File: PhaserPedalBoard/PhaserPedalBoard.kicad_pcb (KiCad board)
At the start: 4 copper layers, 114 parts, among them J1 Footswitch, J2 SWD Header, J5 In, J6 Out, J7 PowerJack, Q1 BC847, Q2 2N7002, Q4 BC847, Q5 BC857, Q6 BC857, SW1 COLOR, SW2 RST, U1 LMR62014XMF, U2 LM13700, U3 LM13700, U4 AMS1117, U5 TL074, U6 STM32L052K6T6, U7 LM2904

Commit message: routing start
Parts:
- moved R147 5.10 mm to (97.5, 84.5), turned to 0 degrees
- moved C123 3.68 mm to (118.8, 109.7)
- moved Q6 1.69 mm to (66.2, 92.3)
- moved C122 1.56 mm to (115.8, 112.1)
- moved R144 1.56 mm to (115.8, 108.8)
- moved R145 1.56 mm to (111.9, 108.8)
- moved C124 1.56 mm to (109.9, 100.9)
- moved D1 1.56 mm to (116.5, 105.3)
- moved L1 1.56 mm to (115.9, 100.6)
- moved R146 1.56 mm to (109.9, 104.8)
- moved U1 1.56 mm to (113.1, 104.8)
- moved R23 0.68 mm to (95.0, 88.0)
- moved R47 0.53 mm to (69.0, 66.0)
- moved C4 0.39 mm to (92.2, 58.5)
- moved R3 0.29 mm to (78.8, 114.0)
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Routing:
- net +3.3V: track 0.00 -> 65.8 mm
- net /Analog/VB: track 0.00 -> 59.9 mm
- net +12VA: track 0.00 -> 58.3 mm, vias 0 -> 1
- net +3.3VA: track 0.00 -> 54.9 mm
- net VCC: track 0.00 -> 36.3 mm
- net /Analog/Stg2: track 0.00 -> 28.3 mm
- net SWDIO: track 0.00 -> 27.3 mm
- net SWCLK: track 0.00 -> 24.9 mm
- net +12V: track 0.00 -> 20.3 mm
- net Net-(Q4-C): track 0.00 -> 17.2 mm
- net Net-(U3A--): track 0.00 -> 15.6 mm
- net /Digital/BypLED: track 0.00 -> 15.2 mm
- net /Analog/InGainIn: track 0.00 -> 14.8 mm
- net DAC_OUT: track 0.00 -> 14.4 mm
- net Net-(U5C-+): track 0.00 -> 13.2 mm
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- added copper zone on B.Cu, net GND
- added copper zone on F.Cu, net GND
- added copper zone on In1.Cu, net GND
- added copper zone on In2.Cu, net GND

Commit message: more routing
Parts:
- moved R26 1.97 mm to (92.8, 98.5)
- moved TP2 0.45 mm to (94.1, 112.1)
- moved R23 0.38 mm to (95.4, 87.9)
- moved R7 0.34 mm to (64.5, 111.2)
- moved R38 0.33 mm to (77.7, 109.7)
- moved R12 0.27 mm to (74.5, 95.1)
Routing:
- net /Analog/In1: track 4.08 -> 58.0 mm, vias 0 -> 3
- net /Analog/Stg4: track 0.00 -> 49.0 mm, vias 0 -> 2
- net DAC_OUT: track 14.4 -> 55.8 mm, vias 0 -> 1
- net NRST: track 3.37 -> 43.5 mm, vias 0 -> 1
- net /Analog/VB: track 59.9 -> 90.4 mm, vias 0 -> 2
- net +3.3V: track 65.8 -> 93.8 mm
- net /Analog/Stg3: track 0.00 -> 26.9 mm, vias 0 -> 2
- net /Digital/SpeedADC: track 0.00 -> 24.0 mm, vias 0 -> 2
- net Net-(U5A-+): track 0.00 -> 22.4 mm
- net Net-(SW1-C): track 0.00 -> 21.1 mm, vias 0 -> 1
- net +12VA: track 58.3 -> 77.0 mm, vias 1 -> 2
- net FX_OUT: track 0.00 -> 17.8 mm, vias 0 -> 1
- net /Analog/Stg1: track 4.63 -> 21.8 mm
- net Net-(U5D--): track 0.00 -> 8.41 mm
- net Net-(SW1-B): track 0.00 -> 7.50 mm
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
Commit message: routed, DRC passing
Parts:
- removed TP5: DAC, TestPoint:TestPoint_THTPad_D2.0mm_Drill1.0mm_VAL
- added RV3: 10kB, Potentiometer_THT:Potentiometer_Alpha_RV16AF_42_Single_Long, F.Cu at (74.1, 113.7)
- added TP3: DAC, TestPoint:TestPoint_THTPad_D2.0mm_Drill1.0mm_VAL, F.Cu at (88.0, 111.1)
- moved TP7 21.9 mm to (84.0, 76.8), turned to -90 degrees
- moved C1 11.5 mm to (104.0, 88.0), turned to -90 degrees
- moved R7 10.3 mm to (63.9, 100.8), turned to 90 degrees
- moved R30 9.97 mm to (74.3, 105.4), turned to -90 degrees
- moved R22 9.71 mm to (98.6, 78.3), turned to 90 degrees
- moved R38 8.84 mm to (72.9, 102.3), turned to 0 degrees
- moved C6 6.93 mm to (94.6, 78.2), turned to -90 degrees
- moved R20 6.88 mm to (91.0, 78.2)
- moved R21 6.88 mm to (87.7, 78.2)
- moved R23 6.88 mm to (99.0, 82.0)
- moved R24 6.88 mm to (91.1, 89.5)
- moved R25 6.88 mm to (87.7, 89.6)
- moved R27 6.88 mm to (98.6, 86.4)
- moved U3 6.88 mm to (91.5, 83.9)
- moved C14 6.88 mm to (94.6, 89.5)
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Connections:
- U5 pad 12: DAC_OUT -> Net-(U5D-+)
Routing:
- net FX_OUT: track 17.8 -> 110.3 mm, vias 1 -> 3
- net +12VA: track 77.0 -> 166.4 mm, vias 2 -> 5
- net FX_IN: track 11.5 -> 100.3 mm
- net BYP_IN: track 7.43 -> 90.9 mm, vias 0 -> 2
- net TAP_IN: track 7.75 -> 91.0 mm, vias 0 -> 2
- net /Analog/VB: track 90.4 -> 143.0 mm
- net DAC_OUT: track 55.8 -> 92.6 mm, vias 1 -> 2
- net /Analog/A: track 10.0 -> 32.9 mm, vias 0 -> 2
- net /Digital/ShapeADC: track 3.72 -> 25.1 mm, vias 0 -> 2
- net +3.3VA: track 54.9 -> 73.8 mm, vias 0 -> 1
- net Net-(U5D-+): track 0.00 -> 18.6 mm
- net /Analog/Stg4: track 49.0 -> 67.2 mm
- net NRST: track 43.5 -> 60.2 mm
- net Net-(SW1-C): track 21.1 -> 36.6 mm
- net /Analog/Stg1: track 21.8 -> 36.9 mm
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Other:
- board outline added: 61 x 80 mm

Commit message: routing tweaks
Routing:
- net /Analog/Stg4: track 67.2 -> 60.7 mm
- net /Analog/VB: track 143.0 -> 144.5 mm
- net FX_IN: track 100.3 -> 98.9 mm
- net TAP_IN: track 91.0 -> 91.6 mm
- net GND: vias 61 -> 94

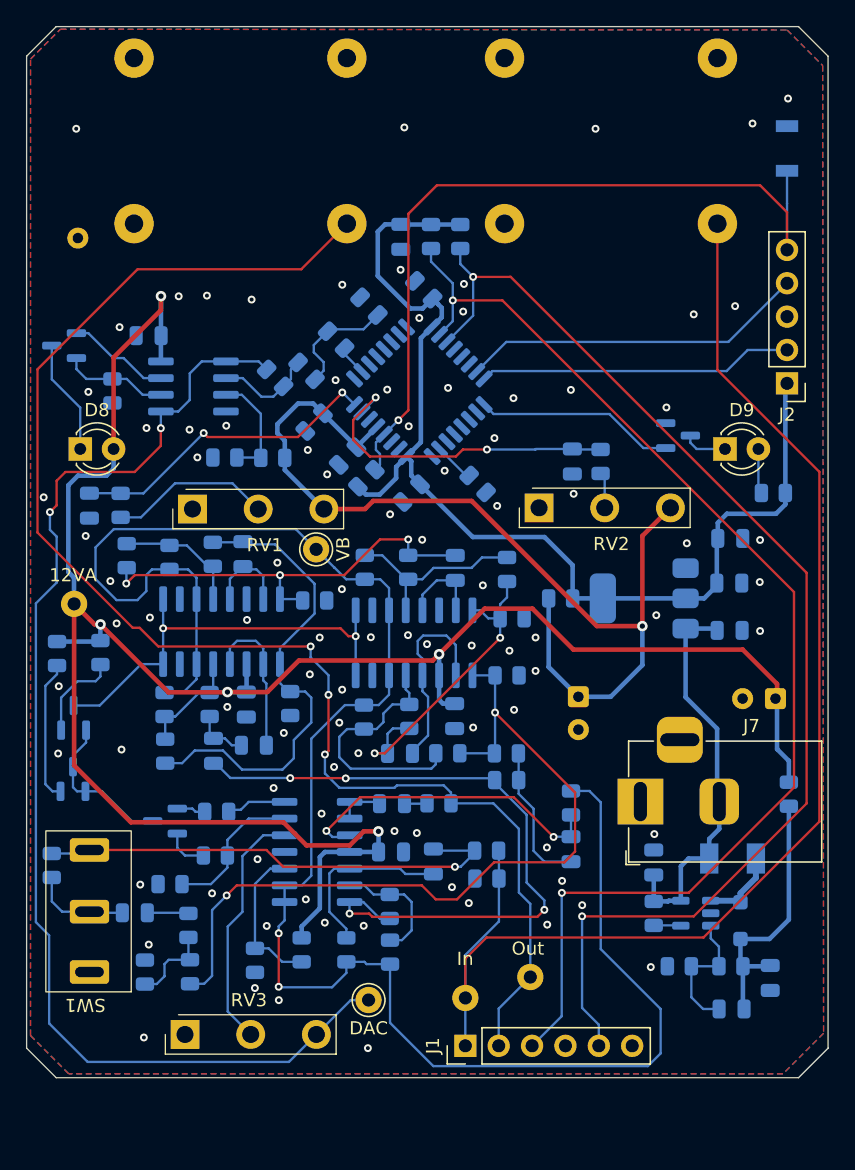
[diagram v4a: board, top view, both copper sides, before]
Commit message: tap tempo shell
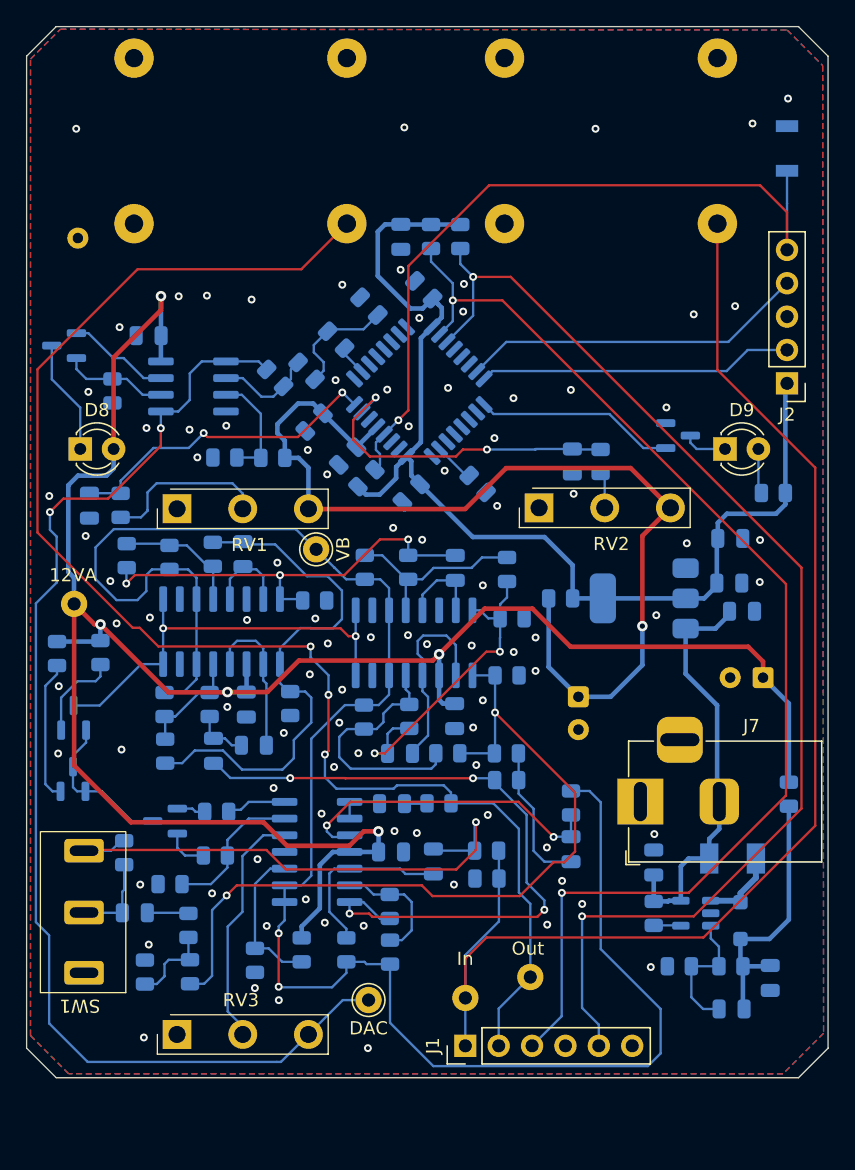
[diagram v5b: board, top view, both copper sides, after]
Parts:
- moved R7 5.59 mm to (69.4, 99.9)
- moved C12 1.86 mm to (118.0, 86.5)
- moved C18 1.73 mm to (116.5, 81.5)
- moved RV1 1.18 mm to (73.5, 73.7)
- moved RV3 0.61 mm to (73.5, 113.7)
- moved SW1 0.42 mm to (69.8, 110.8)
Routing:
- net Net-(SW1-C): track 36.6 -> 42.3 mm
- net /Analog/Stg1: track 36.9 -> 41.0 mm
- net NRST: track 60.2 -> 57.9 mm
- net +3.3VA: track 73.8 -> 75.5 mm
- net VCC: track 30.5 -> 32.0 mm
- net DAC_OUT: track 93.0 -> 91.9 mm
- net Net-(SW1-B): track 7.55 -> 6.73 mm
- net /Analog/Stg3: track 24.4 -> 25.0 mm
- net /Digital/SpeedADC: track 24.0 -> 24.6 mm
- net BYP_IN: track 91.3 -> 90.8 mm

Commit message: routing w DRC passing
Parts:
- removed C21: 10u, Capacitor_SMD:C_0805_2012Metric
- removed R42: 2k2, Resistor_SMD:R_0805_2012Metric
- removed R7: 270k, Resistor_SMD:R_0805_2012Metric
- removed SW1: COLOR, Button_Switch_THT:SW_SPDT_Dailywell_Mini_1M
- added RV4: 10kB, Potentiometer_THT:Potentiometer_Alpha_RV16AF_42_Single_Long, F.Cu at (72.3, 105.8)
- C1: value 220u -> 100u; footprint Capacitor_THT:CP_Radial_D7.5mm_P2.50mm -> Capacitor_THT:CP_Radial_D6.3mm_P2.50mm
- J7, TP3, TP7: moved to B.Cu
- R28: value 4k7 -> 3k3
- R29, R38: value 3k3 -> 4k7
- moved J8 54.2 mm to (119.1, 42.7), turned to -90 degrees
- moved Q5 53.5 mm to (118.9, 97.6)
- moved Q6 53.4 mm to (118.9, 92.8)
- moved R40 52.2 mm to (114.7, 98.3), turned to 180 degrees
- moved R41 47.9 mm to (114.6, 93.8), turned to 180 degrees
- moved Q4 47.1 mm to (119.3, 103.2), turned to 0 degrees
- moved R38 43.1 mm to (116.0, 101.3), turned to -90 degrees
- moved C12 40.1 mm to (89.3, 114.5), turned to -90 degrees
- moved R48 36.3 mm to (95.6, 44.6), turned to 90 degrees
- moved TP6 36.2 mm to (85.3, 111.3)
- moved R5 32.8 mm to (65.3, 110.3), turned to -90 degrees
- moved D9 31.8 mm to (93.0, 46.4), turned to 90 degrees
- moved R1 31.5 mm to (92.6, 110.9), turned to 180 degrees
- moved R6 30.5 mm to (68.4, 110.3), turned to 90 degrees
- moved RV3 30.2 mm to (102.5, 105.8)
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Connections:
- C3 pad 1: Net-(SW1-C) -> Net-(C3-Pad1)
- C9 pad 1: Net-(SW1-B) -> Net-(C3-Pad1)
- R10 pad 1: Net-(U5B--) -> Net-(U5D--)
- R29 pad 1: Net-(R28-Pad2) -> Net-(R29-Pad1)
- R30 pad 2: Net-(R28-Pad2) -> Net-(R30-Pad2)
- R38 pad 2: Net-(U5D--) -> Net-(Q4-E)
- R6 pad 2: Net-(SW1-C) -> Net-(C3-Pad1)
- R9 pad 2: Net-(U5B--) -> Net-(U5D--)
- RV3 pad 2: Net-(U5D-+) -> Net-(U5B-+)
- U5 pad 12: Net-(U5D-+) -> /Analog/InGainIn
- U5 pad 14: Net-(R39-Pad1) -> /Analog/In1
- U5 pad 5: /Analog/InGainIn -> Net-(U5B-+)
- U5 pad 6: Net-(U5B--) -> Net-(Q4-E)
- U5 pad 7: /Analog/In1 -> Net-(R39-Pad1)
- U6 pad 14: unconnected-(U6-PB0-Pad14) -> /Digital/BypLED
- U6 pad 25: /Digital/BypLED -> unconnected-(U6-PA15-Pad25)
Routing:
- net /Analog/A: track 32.9 -> 81.1 mm, vias 2 -> 3
- net Net-(SW1-C): track 42.3 -> 0.00 mm, vias 1 -> 0
- net FX_IN: track 98.6 -> 137.2 mm
- net DAC_OUT: track 91.9 -> 128.9 mm, vias 2 -> 1
- net /Analog/VB: track 144.5 -> 110.7 mm, vias 2 -> 4
- net VCC: track 32.0 -> 64.7 mm, vias 0 -> 1
- net NRST: track 57.9 -> 88.3 mm
- net TAP_IN: track 91.3 -> 120.4 mm, vias 2 -> 3
- net /Analog/In1: track 53.0 -> 26.4 mm, vias 4 -> 0
- net Net-(C3-Pad1): track 0.00 -> 26.3 mm
- net Net-(Q4-B): track 2.19 -> 25.8 mm
- net BYP_IN: track 90.8 -> 114.1 mm, vias 2 -> 3
- net Net-(Q4-E): track 3.31 -> 25.6 mm
- net Net-(U5D-+): track 18.6 -> 0.00 mm
- net Net-(U5B-+): track 0.00 -> 15.4 mm, vias 0 -> 1
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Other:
- board size 61 x 80 mm -> 61 x 85 mm

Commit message: minor niceties
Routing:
- net FX_IN: track 137.2 -> 140.2 mm
- net +3.3VA: track 79.1 -> 77.7 mm
- net Net-(C8-Pad2): track 11.9 -> 11.3 mm
- net GND: vias 33 -> 81

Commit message: routing improvements
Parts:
- moved Q2 0.86 mm to (92.9, 50.6)
- moved R48 0.86 mm to (95.5, 45.4)
- moved D9 0.86 mm to (92.9, 47.2)
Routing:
- net /Analog/Stg4: track 63.5 -> 59.5 mm
- net NRST: track 87.9 -> 84.5 mm, vias 1 -> 2
- net TAP_IN: track 120.4 -> 117.5 mm, vias 3 -> 1
- net FX_IN: track 140.2 -> 137.4 mm
- net /Analog/Stg1: track 30.9 -> 33.5 mm
- net FX_OUT: track 101.2 -> 100.3 mm, vias 2 -> 1
- net +3.3V: track 98.4 -> 97.6 mm
- net /Analog/A: track 81.1 -> 80.4 mm
- net /Digital/BypLED: track 15.5 -> 14.9 mm
- net BYP_IN: track 114.1 -> 113.6 mm, vias 3 -> 1
- net GND: vias 81 -> 87
